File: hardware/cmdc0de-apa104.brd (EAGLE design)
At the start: 100.6 x 72.6 mm, 128 parts, among them IC1 ATTINY13A-SSU, J1 1x8 header

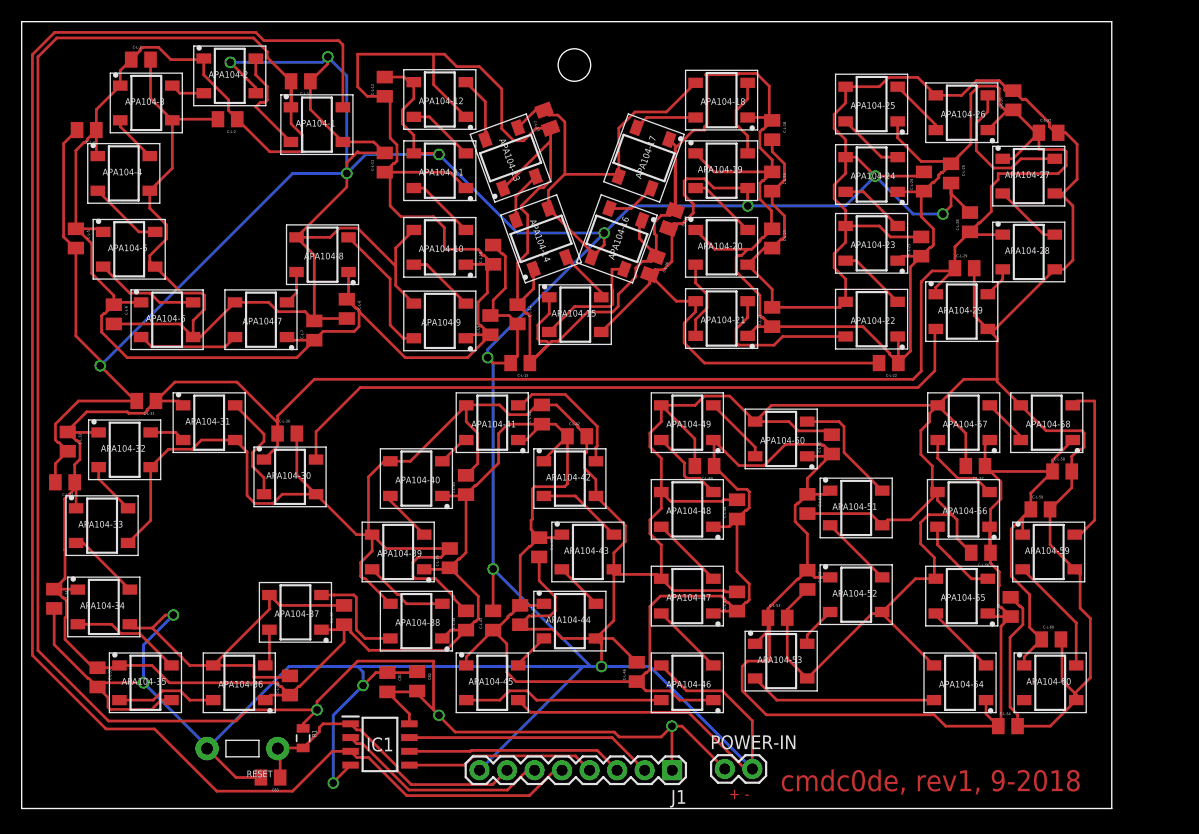
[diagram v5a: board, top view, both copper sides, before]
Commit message: more tweaking to get distances right
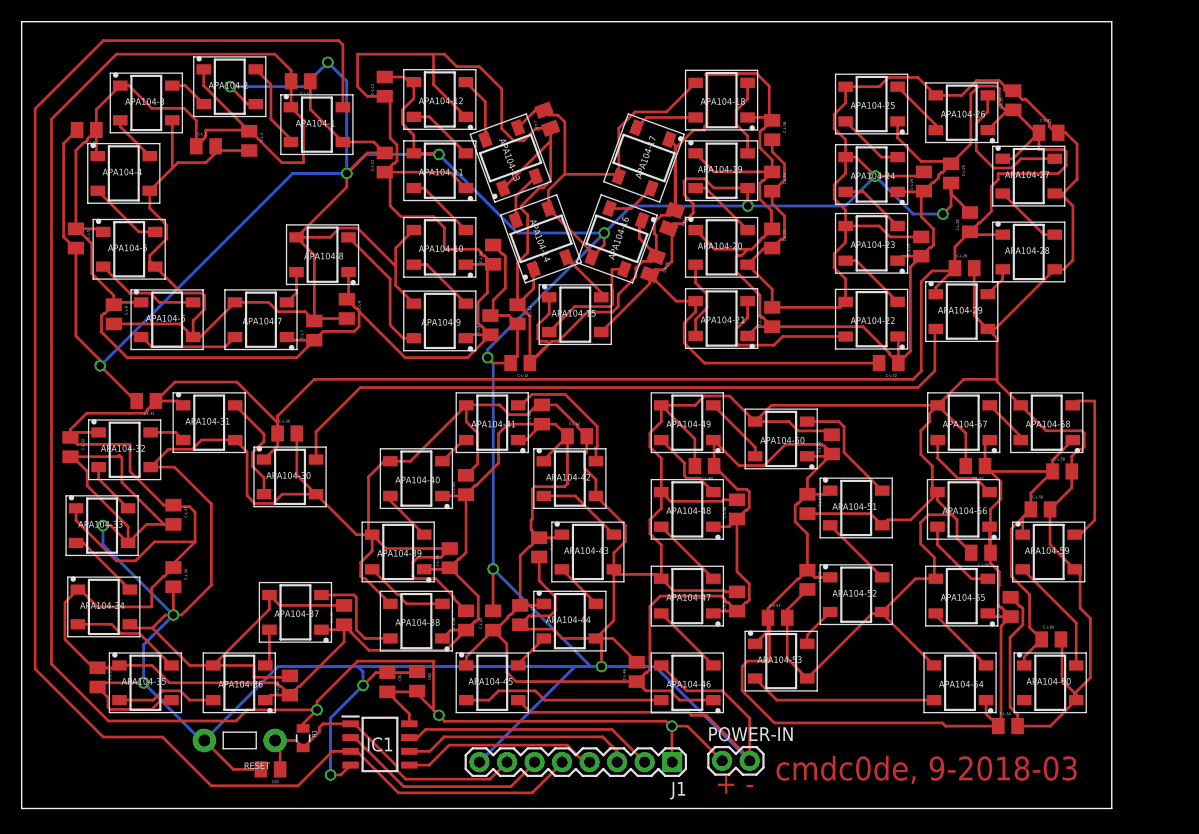
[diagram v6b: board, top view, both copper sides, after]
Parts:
- moved C-L-34 11.2 mm to (14.0, 48.8)
- moved C-L-33 10.4 mm to (14.0, 54.5), turned to 270 degrees
- moved C-L-3 10.0 mm to (17.0, 88.5)
- moved C-L-2 2.83 mm to (21.0, 89.0), turned to 270 degrees
- moved APA104-2 1.00 mm to (19.2, 94.0)
- moved POWER-IN 0.79 mm to (64.6, 31.8)
- moved RESET 0.79 mm to (20.1, 33.7)
- moved C83 0.75 mm to (23.0, 31.0)
- moved J1 0.75 mm to (60.0, 31.7)
- moved C-L-32 0.56 mm to (4.50, 60.8)
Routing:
- net VDD: track 1084.5 -> 1108.5 mm
- net GND: track 1176.5 -> 1198.5 mm, vias 16 -> 17
- net GPIO_APA104_DATA: track 149.4 -> 145.8 mm
- net N$31: track 10.2 -> 8.04 mm
- net PB1-MISO: track 20.0 -> 21.3 mm
- net PB0-MOSI: track 17.5 -> 18.0 mm
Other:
- board text added: "cmdc0de, 9-2018-03"
- board text removed: "cmdc0de, rev1, 9-2018"

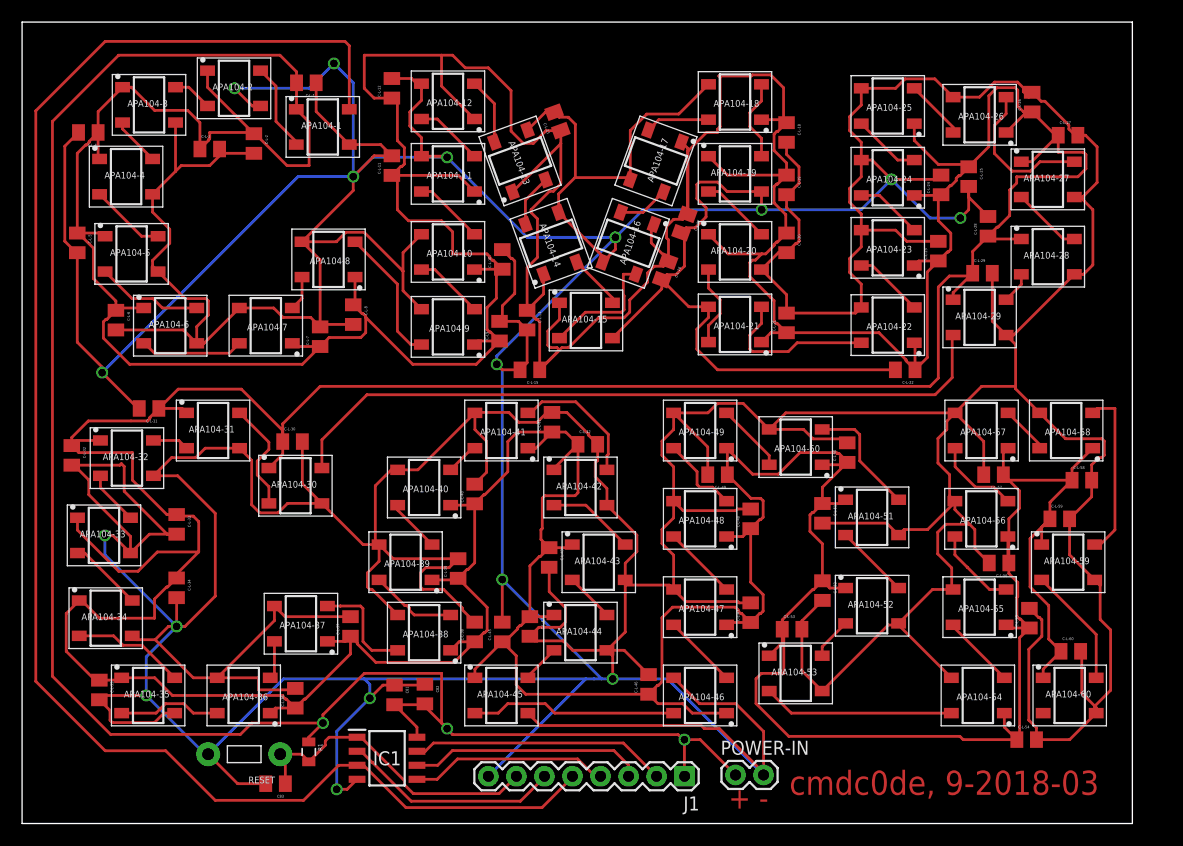
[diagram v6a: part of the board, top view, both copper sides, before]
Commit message: moved wires farther apart again
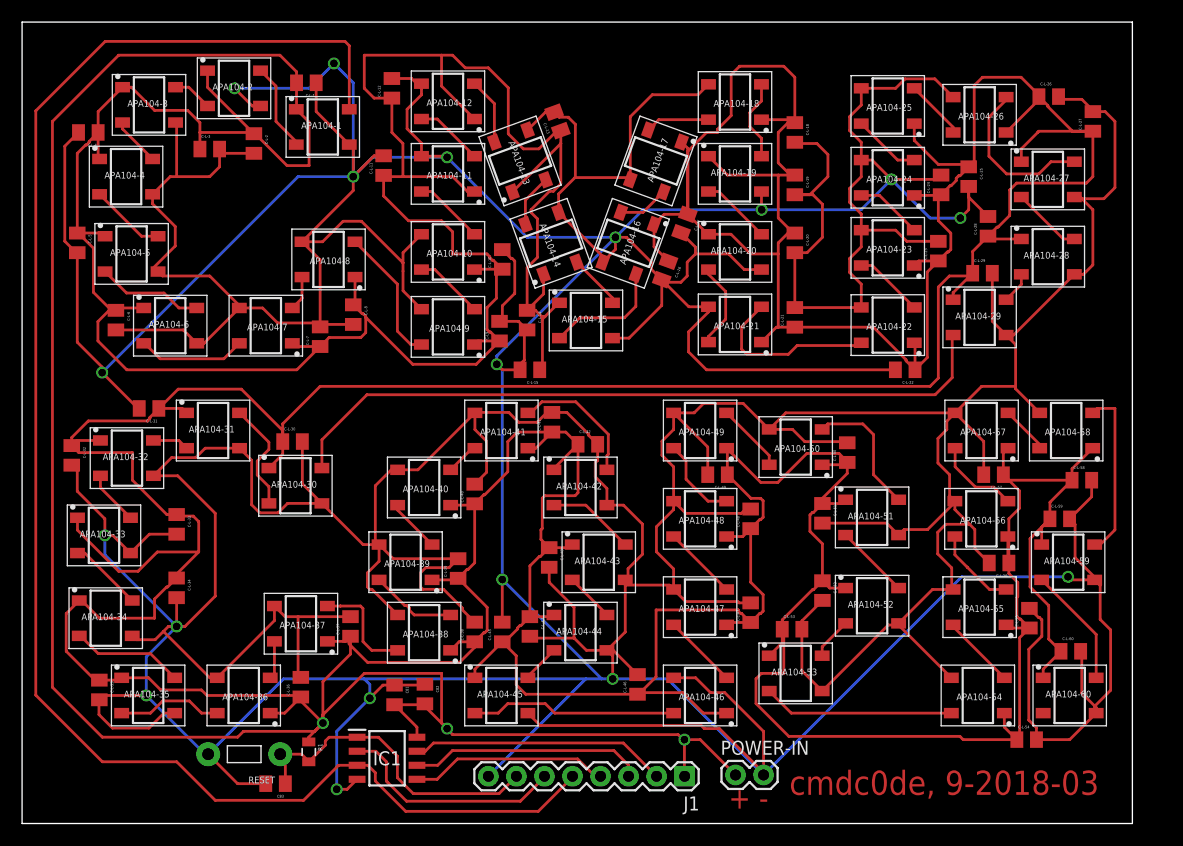
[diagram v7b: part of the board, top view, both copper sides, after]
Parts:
- moved C-L-27 2.57 mm to (97.0, 91.0), turned to 90 degrees
- moved C-L-26 1.58 mm to (93.0, 93.2), turned to 0 degrees
- moved C-L-36 1.12 mm to (25.2, 39.8)
- moved C-L-46 1.00 mm to (55.8, 40.0)
- moved C-L-21 0.90 mm to (70.0, 73.2)
- moved C-L-11 0.75 mm to (32.8, 87.0)
- moved C-L-18 0.75 mm to (70.0, 90.0)
- moved C-L-19 0.75 mm to (70.0, 85.2)
- moved C-L-20 0.75 mm to (70.0, 80.0)
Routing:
- net GND: track 1198.5 -> 1204.4 mm, vias 17 -> 18
- net GPIO_APA104_DATA: track 145.8 -> 147.3 mm
- net N$19: track 14.8 -> 16.1 mm
- net PB3: track 19.9 -> 21.0 mm
- net N$41: track 11.0 -> 12.1 mm
- net VDD: track 1108.5 -> 1107.3 mm
- net N$24: track 13.8 -> 14.9 mm
- net RESET: track 28.7 -> 29.6 mm

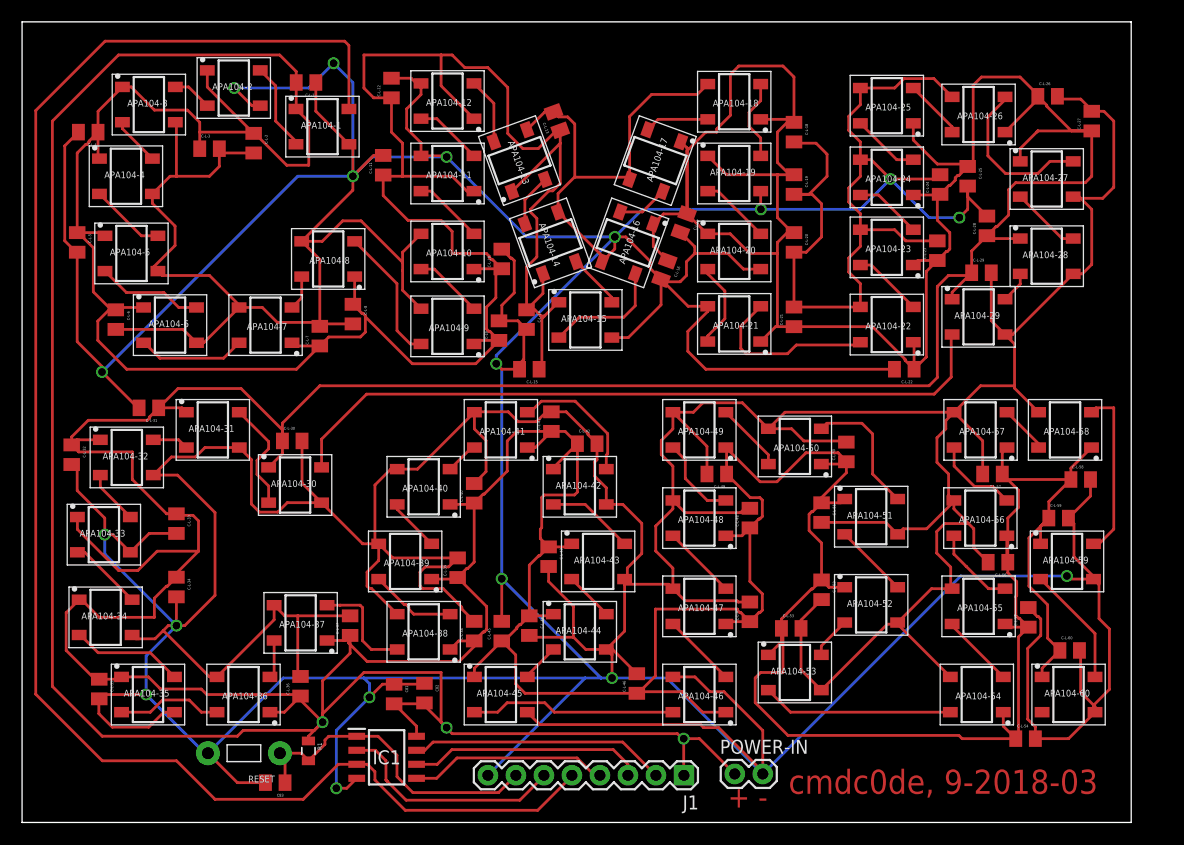
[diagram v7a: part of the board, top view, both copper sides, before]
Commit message: new dru file with real limits for voltera
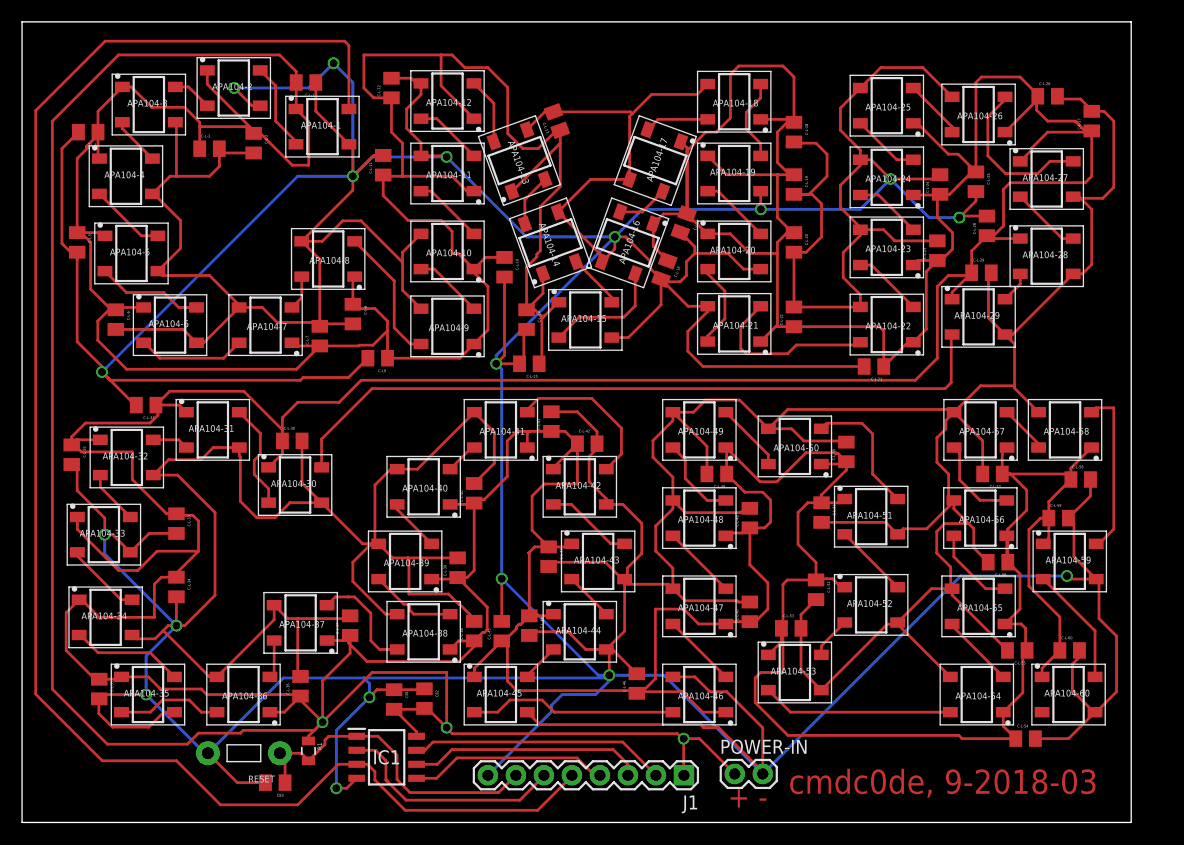
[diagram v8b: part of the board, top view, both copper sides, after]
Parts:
- moved C-L9 11.3 mm to (32.2, 69.5), turned to 180 degrees
- moved C-L-55 3.16 mm to (90.2, 43.0), turned to 180 degrees
- moved C-L-22 2.76 mm to (77.2, 68.8)
- moved C-L-25 0.90 mm to (86.5, 85.5)
- moved C-L-10 0.79 mm to (43.8, 77.8), turned to 270 degrees
- moved C-L-15 0.50 mm to (46.0, 69.0)
- moved C-L-52 0.50 mm to (72.0, 48.5)
- moved C81 0.50 mm to (33.7, 38.5)
- moved C82 0.50 mm to (36.5, 38.6)
- moved C-L-31 0.35 mm to (11.2, 65.2)
- moved APA104-59 0.25 mm to (95.0, 51.1)
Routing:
- net GND: track 1204.4 -> 1220.6 mm
- net N$30: track 12.2 -> 14.6 mm
- net VDD: track 1107.3 -> 1106.2 mm
